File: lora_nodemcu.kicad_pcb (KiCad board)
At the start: 4 copper layers, 25.8 x 32.9 mm, 17 parts, among them U1 RFM95, U2 LM1117-3.3, U3 WeMos_mini

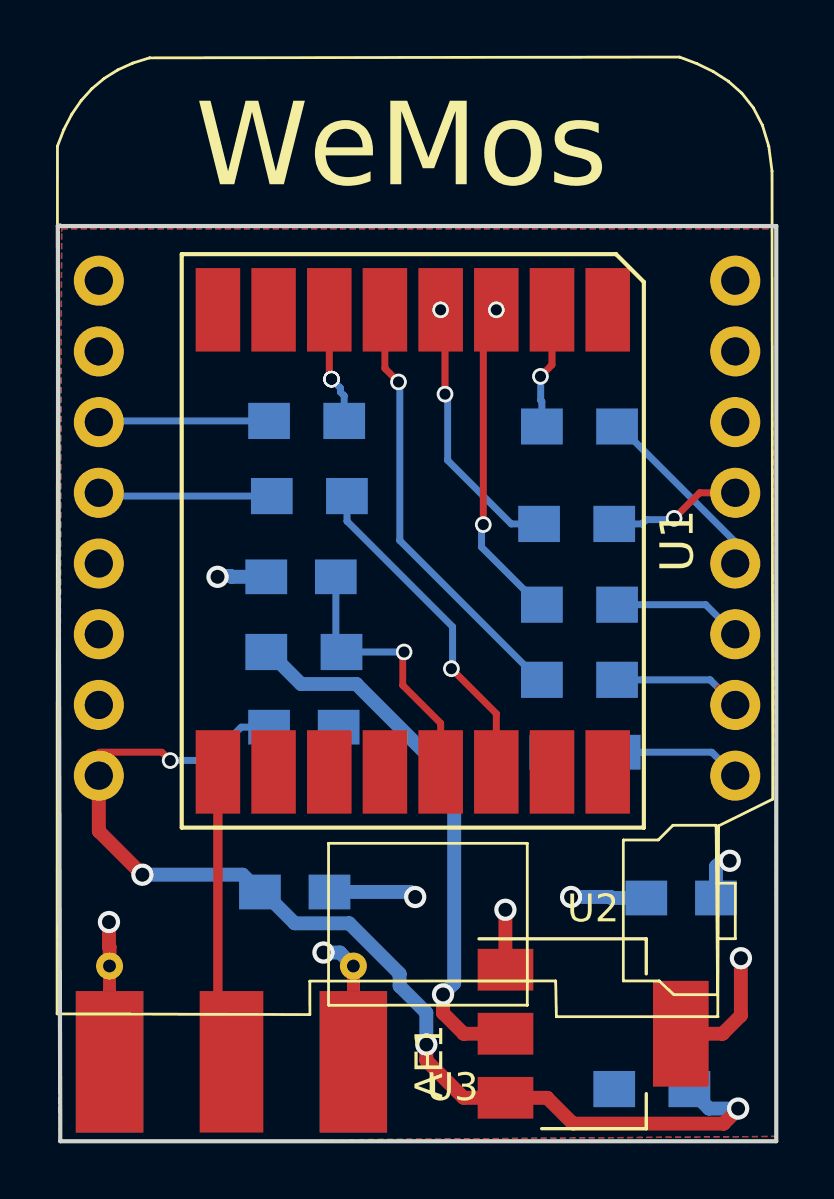
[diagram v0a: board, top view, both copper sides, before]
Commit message: fixed non connect on schematic and moved decoupling caps closer
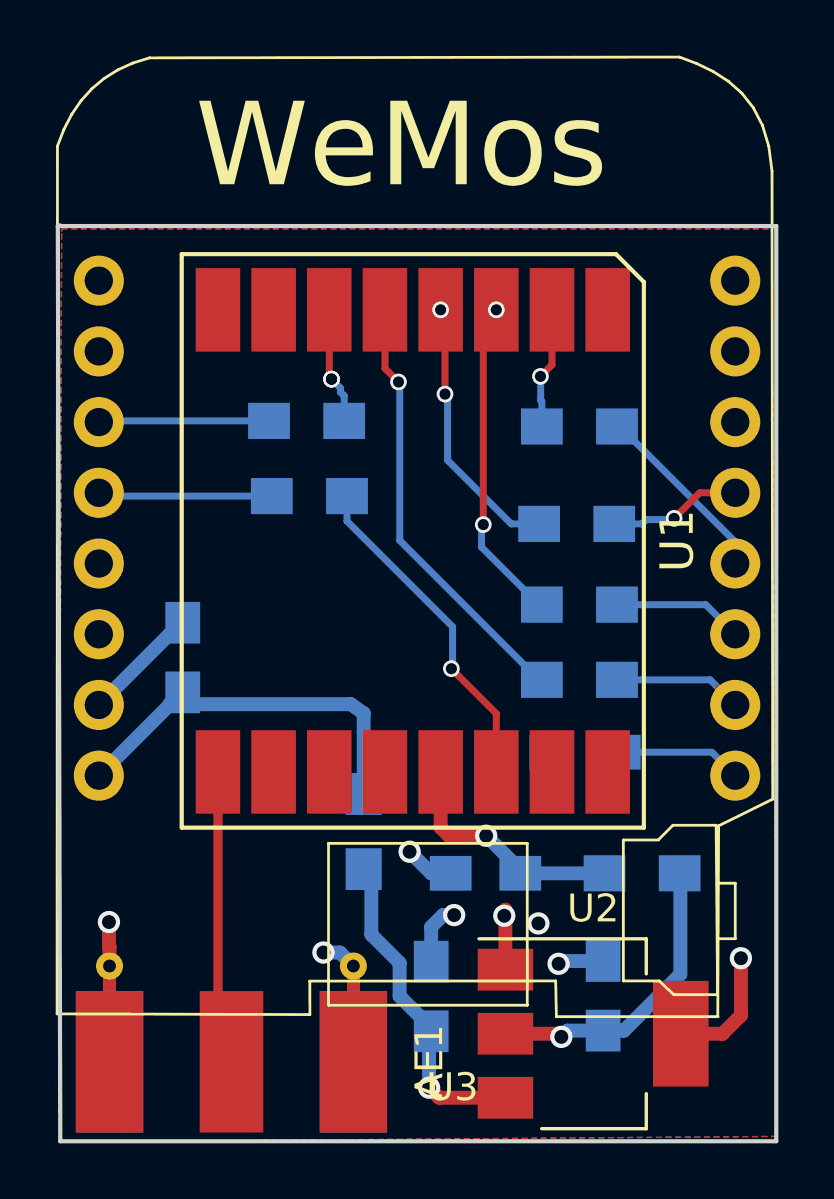
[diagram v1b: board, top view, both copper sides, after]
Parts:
- moved L1 14.5 mm to (156.8, 98.2), turned to 0 degrees
- moved L2 13.9 mm to (146.8, 96.8), turned to 270 degrees
- moved C3 12.5 mm to (151.1, 98.2)
- moved C1 6.18 mm to (149.2, 102.7), turned to 270 degrees
- moved C4 5.02 mm to (140.2, 90.5), turned to 270 degrees
- moved C2 4.49 mm to (155.3, 102.7), turned to 270 degrees
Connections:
- net Net-(C3-Pad1) renamed /RF95_3V3
- C4 pad 2: Net-(C4-Pad2) -> /wemos_5V
- L2 pad 1: Net-(L2-Pad1) -> /wemos_5V
- U3 pad 1: Net-(C4-Pad2) -> /wemos_5V
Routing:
- net +5V: track 32.8 -> 11.8 mm, vias 3 -> 1
- net /wemos_5V: track 0.00 -> 13.6 mm
- net +3V3: track 25.9 -> 14.8 mm, vias 3 -> 2
- net Net-(C4-Pad2): track 7.32 -> 0.00 mm, vias 1 -> 0
- net GND: track 19.5 -> 21.4 mm, vias 6 -> 7
- net /RF95_3V3: track 9.93 -> 8.64 mm

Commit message: added ground vias
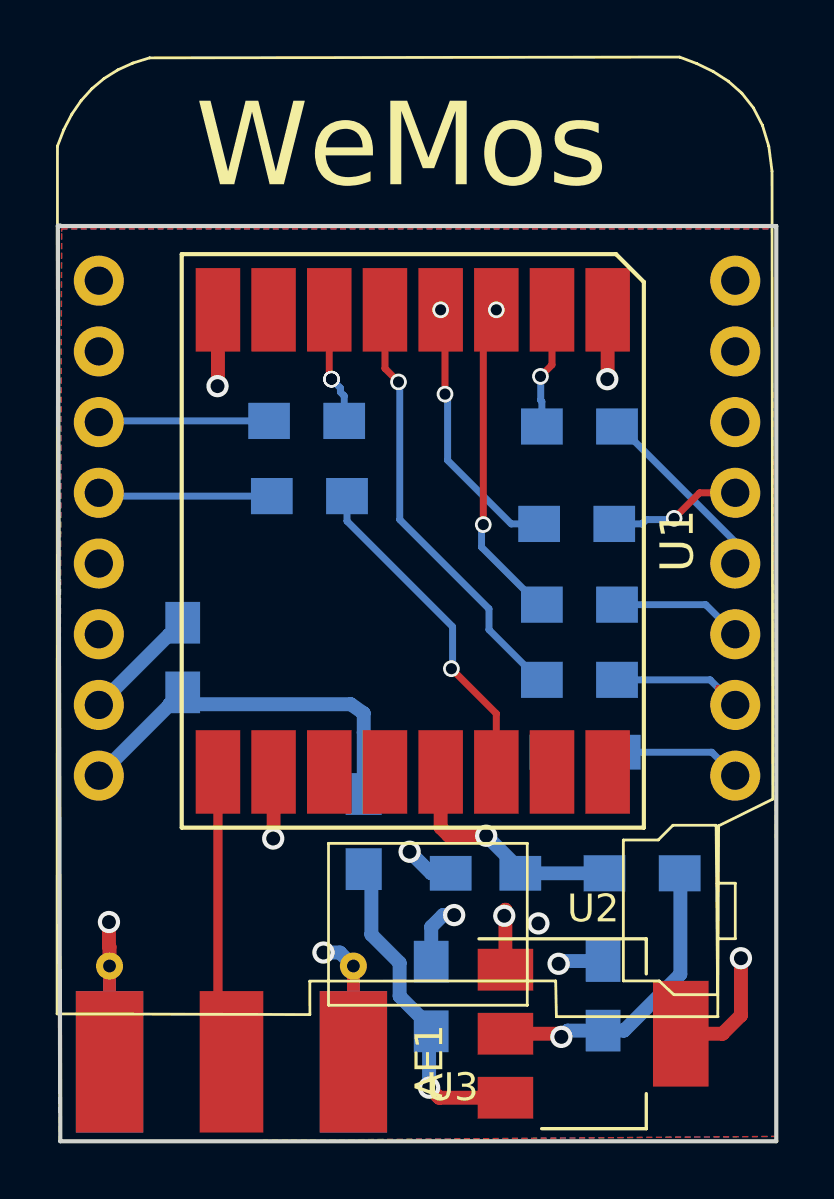
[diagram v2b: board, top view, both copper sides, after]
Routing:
- net GND: track 21.4 -> 29.0 mm, vias 7 -> 10
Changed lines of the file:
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@@
     (thickness 1.2)
     (drawings 10)
-    (tracks 132)
+    (tracks 143)
     (zones 0)
     (modules 17)
@@
   )
   (setup
-    (last_trace_width 0.5)
+    (last_trace_width 0.25)
     (user_trace_width 0.5)
     (trace_clearance 0.2)
@@
       (effects (font (size 1 1) (thickness 0.15)) (justify mirror))
     )
+    (fp_line (start 2.25 -0.87) (end -2.25 -0.87) (layer B.CrtYd) (width 0.05))
+    (fp_line (start 2.25 -0.87) (end 2.25 0.88) (layer B.CrtYd) (width 0.05))
+    (fp_line (start -2.25 0.88) (end -2.25 -0.87) (layer B.CrtYd) (width 0.05))
+    (fp_line (start -2.25 0.88) (end 2.25 0.88) (layer B.CrtYd) (width 0.05))
+    (fp_line (start -0.5 -0.85) (end 0.5 -0.85) (layer B.SilkS) (width 0.12))
+    (fp_line (start 0.5 0.85) (end -0.5 0.85) (layer B.SilkS) (width 0.12))
+    (fp_line (start -1 0.62) (end 1 0.62) (layer B.Fab) (width 0.1))
+    (fp_line (start 1 0.62) (end 1 -0.62) (layer B.Fab) (width 0.1))
+    (fp_line (start 1 -0.62) (end -1 -0.62) (layer B.Fab) (width 0.1))
+    (fp_line (start -1 -0.62) (end -1 0.62) (layer B.Fab) (width 0.1))
     (fp_text user %R (at 0 1.75 270) (layer B.Fab)
       (effects (font (size 1 1) (thickness 0.15)) (justify mirror))
     )
-    (fp_line (start -1 -0.62) (end -1 0.62) (layer B.Fab) (width 0.1))
-    (fp_line (start 1 -0.62) (end -1 -0.62) (layer B.Fab) (width 0.1))
-    (fp_line (start 1 0.62) (end 1 -0.62) (layer B.Fab) (width 0.1))
-    (fp_line (start -1 0.62) (end 1 0.62) (layer B.Fab) (width 0.1))
-    (fp_line (start 0.5 0.85) (end -0.5 0.85) (layer B.SilkS) (width 0.12))
-    (fp_line (start -0.5 -0.85) (end 0.5 -0.85) (layer B.SilkS) (width 0.12))
-    (fp_line (start -2.25 0.88) (end 2.25 0.88) (layer B.CrtYd) (width 0.05))
-    (fp_line (start -2.25 0.88) (end -2.25 -0.87) (layer B.CrtYd) (width 0.05))
-    (fp_line (start 2.25 -0.87) (end 2.25 0.88) (layer B.CrtYd) (width 0.05))
-    (fp_line (start 2.25 -0.87) (end -2.25 -0.87) (layer B.CrtYd) (width 0.05))
-    (pad 1 smd rect (at -1.25 0 270) (size 1.5 1.25) (layers B.Cu B.Mask)
-      (net 14 GND))
     (pad 2 smd rect (at 1.25 0 270) (size 1.5 1.25) (layers B.Cu B.Mask)
       (net 30 /wemos_5V))
+    (pad 1 smd rect (at -1.25 0 270) (size 1.5 1.25) (layers B.Cu B.Mask)
+      (net 14 GND))
     (model Capacitors_SMD.3dshapes/C_0805.wrl
       (at (xyz 0 0 0))
@@
   (segment (start 159.4942 91.6) (end 160.0962 92.202) (width 0.25) (layer F.Cu) (net 5))
   (via (at 160.0962 92.202) (size 0.6) (drill 0.4) (layers F.Cu B.Cu) (net 5))
+  (segment (start 151.25 88.75) (end 151.25 89.5) (width 0.25) (layer B.Cu) (net 6))
+  (segment (start 148.046205 80.646205) (end 148.046205 85.546205) (width 0.25) (layer B.Cu) (net 6))
+  (segment (start 148.046205 85.546205) (end 151.25 88.75) (width 0.25) (layer B.Cu) (net 6))
+  (segment (start 148 80.6) (end 148.046205 80.646205) (width 0.25) (layer B.Cu) (net 6))
+  (segment (start 151.25 89.5) (end 153.05 91.3) (width 0.25) (layer B.Cu) (net 6))
+  (segment (start 153.05 91.3) (end 153.15 91.3) (width 0.25) (layer B.Cu) (net 6))
   (segment (start 148 80.6) (end 147.5138 80.1138) (width 0.25) (layer F.Cu) (net 6))
   (segment (start 147.5138 80.1138) (end 147.5138 78.0092) (width 0.25) (layer F.Cu) (net 6))
-  (segment (start 148.046205 86.296205) (end 148.046205 80.646205) (width 0.25) (layer B.Cu) (net 6))
   (via (at 148 80.6) (size 0.6) (drill 0.4) (layers F.Cu B.Cu) (net 6))
-  (segment (start 148.046205 80.646205) (end 148 80.6) (width 0.25) (layer B.Cu) (net 6))
-  (segment (start 153.15 91.3) (end 153.05 91.3) (width 0.25) (layer B.Cu) (net 6))
-  (segment (start 153.05 91.3) (end 148.046205 86.296205) (width 0.25) (layer B.Cu) (net 6))
   (segment (start 157.9 85.5) (end 158.818 84.582) (width 0.25) (layer F.Cu) (net 7))
   (segment (start 158.818 84.582) (end 160.0962 84.582) (width 0.25) (layer F.Cu) (net 7))
@@
   (segment (start 153.15 88.6) (end 153.05 88.6) (width 0.25) (layer B.Cu) (net 12))
   (segment (start 153.05 88.6) (end 150.983295 86.533295) (width 0.25) (layer B.Cu) (net 12))
+  (segment (start 143.5138 94.6092) (end 143.5138 96.9862) (width 0.5) (layer F.Cu) (net 14))
+  (via (at 143.5 97) (size 0.8) (drill 0.5) (layers F.Cu B.Cu) (net 14))
+  (segment (start 143.5138 96.9862) (end 143.5 97) (width 0.5) (layer F.Cu) (net 14))
+  (segment (start 155.5138 78.0092) (end 155.5138 80.4862) (width 0.5) (layer F.Cu) (net 14))
+  (segment (start 155.5138 80.4862) (end 155.5 80.5) (width 0.5) (layer F.Cu) (net 14))
+  (via (at 155.5 80.5) (size 0.8) (drill 0.5) (layers F.Cu B.Cu) (net 14))
+  (segment (start 141.5138 78.0092) (end 141.5138 80.7362) (width 0.5) (layer F.Cu) (net 14))
+  (segment (start 141.5138 80.7362) (end 141.5 80.75) (width 0.5) (layer F.Cu) (net 14))
+  (via (at 141.5 80.75) (size 0.8) (drill 0.5) (layers F.Cu B.Cu) (net 14))
   (segment (start 155.35 101.4) (end 153.85 101.4) (width 0.5) (layer B.Cu) (net 14))
   (segment (start 153.85 101.4) (end 153.75 101.5) (width 0.5) (layer B.Cu) (net 14))

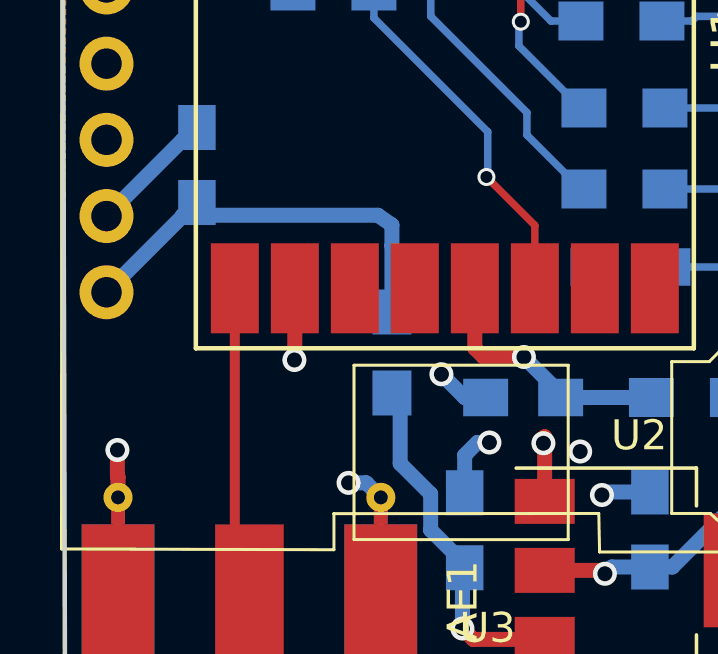
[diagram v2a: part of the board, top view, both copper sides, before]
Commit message: removed vias inside of pads
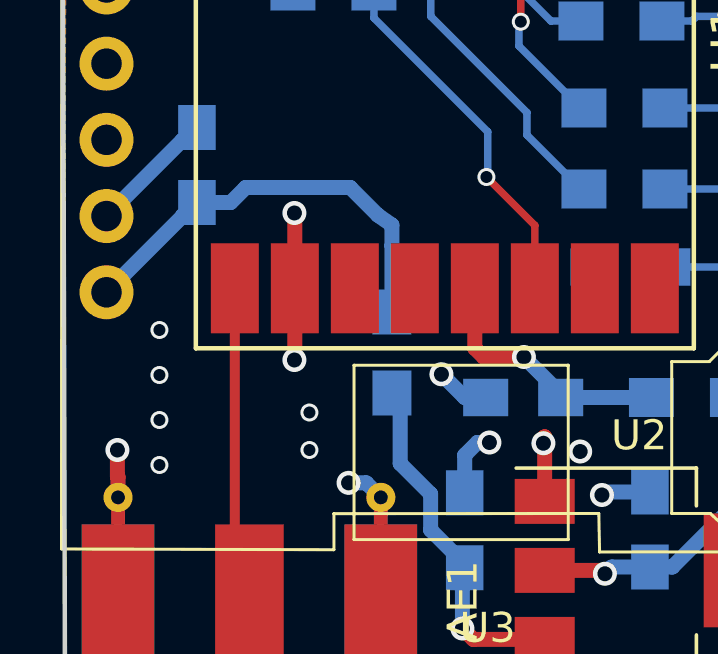
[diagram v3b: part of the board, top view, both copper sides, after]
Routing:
- net GND: track 29.0 -> 31.6 mm, vias 10 -> 17
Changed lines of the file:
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@@
     (thickness 1.2)
     (drawings 10)
-    (tracks 143)
+    (tracks 155)
     (zones 0)
     (modules 17)
@@
   (segment (start 153.15 88.6) (end 153.05 88.6) (width 0.25) (layer B.Cu) (net 12))
   (segment (start 153.05 88.6) (end 150.983295 86.533295) (width 0.25) (layer B.Cu) (net 12))
+  (segment (start 143.5138 94.6092) (end 143.5138 92.1138) (width 0.5) (layer F.Cu) (net 14))
+  (segment (start 143.5138 92.1138) (end 143.5 92.1) (width 0.5) (layer F.Cu) (net 14))
+  (via (at 143.5 92.1) (size 0.8) (drill 0.5) (layers F.Cu B.Cu) (net 14))
+  (via (at 144 98.75) (size 0.6) (drill 0.4) (layers F.Cu B.Cu) (net 14))
+  (via (at 139 97.5) (size 0.6) (drill 0.4) (layers F.Cu B.Cu) (net 14))
+  (via (at 139 96) (size 0.6) (drill 0.4) (layers F.Cu B.Cu) (net 14))
+  (via (at 139 100.5) (size 0.6) (drill 0.4) (layers F.Cu B.Cu) (net 14))
+  (via (at 144 100) (size 0.6) (drill 0.4) (layers F.Cu B.Cu) (net 14))
+  (via (at 139 99) (size 0.6) (drill 0.4) (layers F.Cu B.Cu) (net 14))
   (segment (start 143.5138 94.6092) (end 143.5138 96.9862) (width 0.5) (layer F.Cu) (net 14))
   (via (at 143.5 97) (size 0.8) (drill 0.5) (layers F.Cu B.Cu) (net 14))
@@
   (segment (start 146.38 101.58) (end 146.38 105.02) (width 0.25) (layer B.Cu) (net 14))
   (segment (start 137.62 105.02) (end 137.62 101.58) (width 0.25) (layer B.Cu) (net 14))
-  (segment (start 139.775 92.175) (end 146.285002 92.175) (width 0.5) (layer B.Cu) (net 30))
+  (segment (start 141.875 91.25) (end 145.360002 91.25) (width 0.5) (layer B.Cu) (net 30))
+  (segment (start 145.360002 91.25) (end 146.285002 92.175) (width 0.5) (layer B.Cu) (net 30))
+  (segment (start 140.25 91.75) (end 141.375 91.75) (width 0.5) (layer B.Cu) (net 30))
+  (segment (start 141.375 91.75) (end 141.875 91.25) (width 0.5) (layer B.Cu) (net 30))
   (segment (start 146.75 93.189998) (end 146.75 95.4) (width 0.5) (layer B.Cu) (net 30))
   (segment (start 146.285002 92.175) (end 146.75 92.5) (width 0.5) (layer B.Cu) (net 30))
